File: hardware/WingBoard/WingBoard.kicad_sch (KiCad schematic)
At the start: 27 parts, among them J101 UPDI, J102 UART0, SW101 DIPA, SW103 SW_SPST, U101 ATmega4809-A

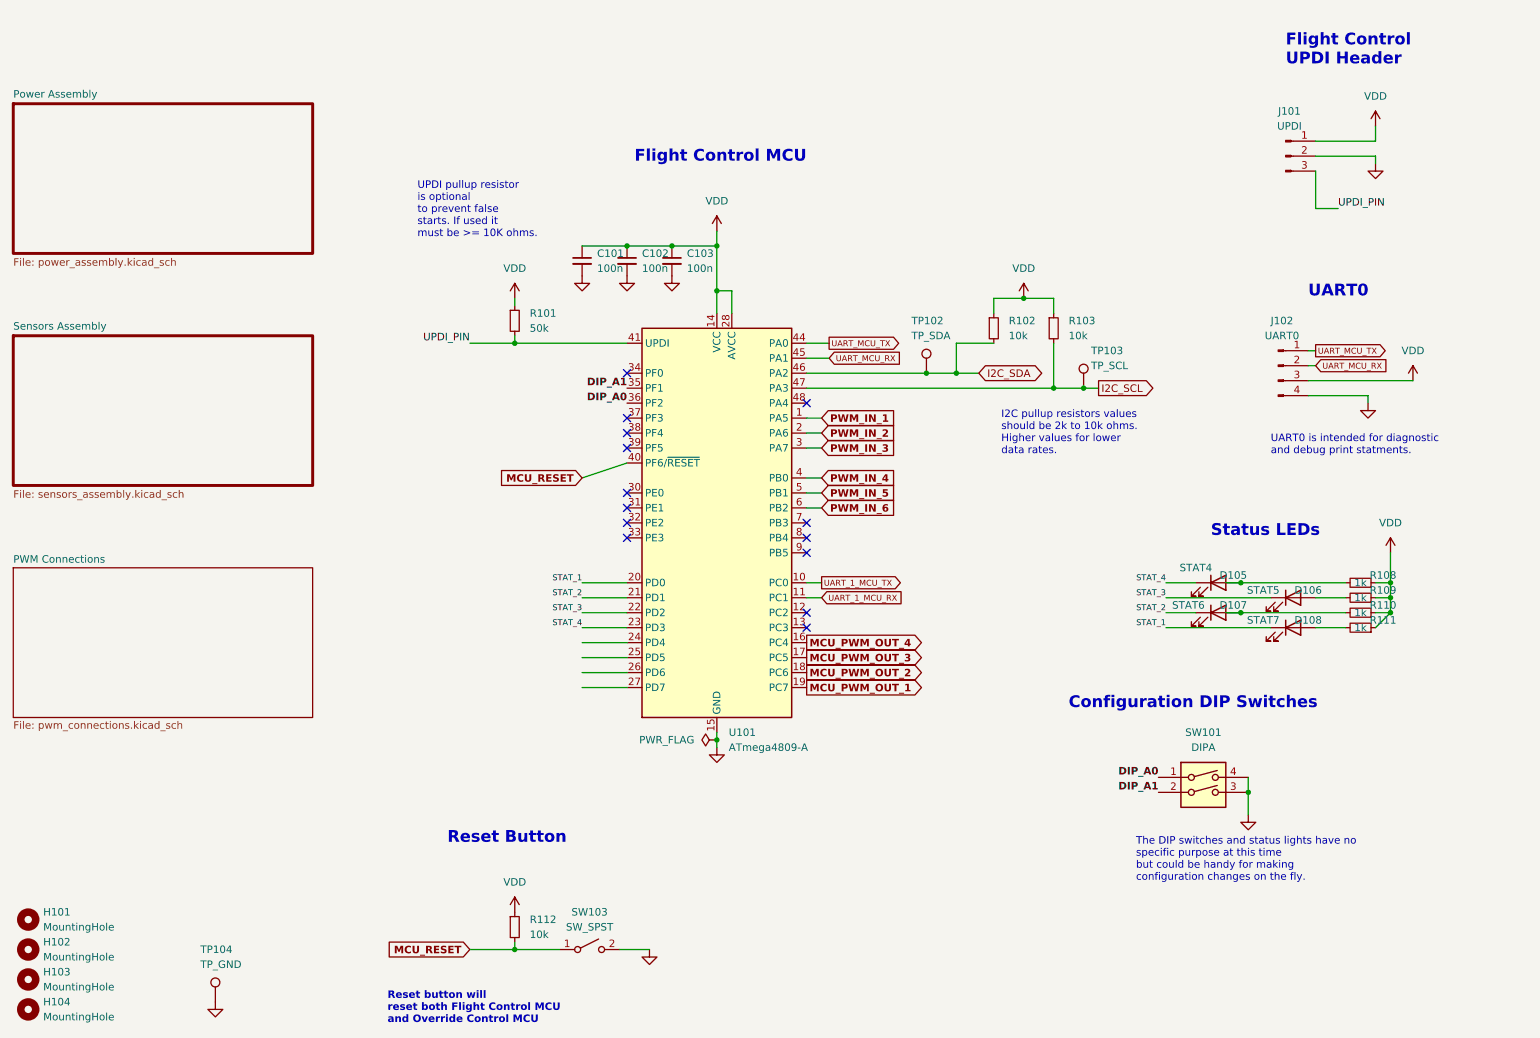
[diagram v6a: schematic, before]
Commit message: Final wingboard v0.1 hardware design.
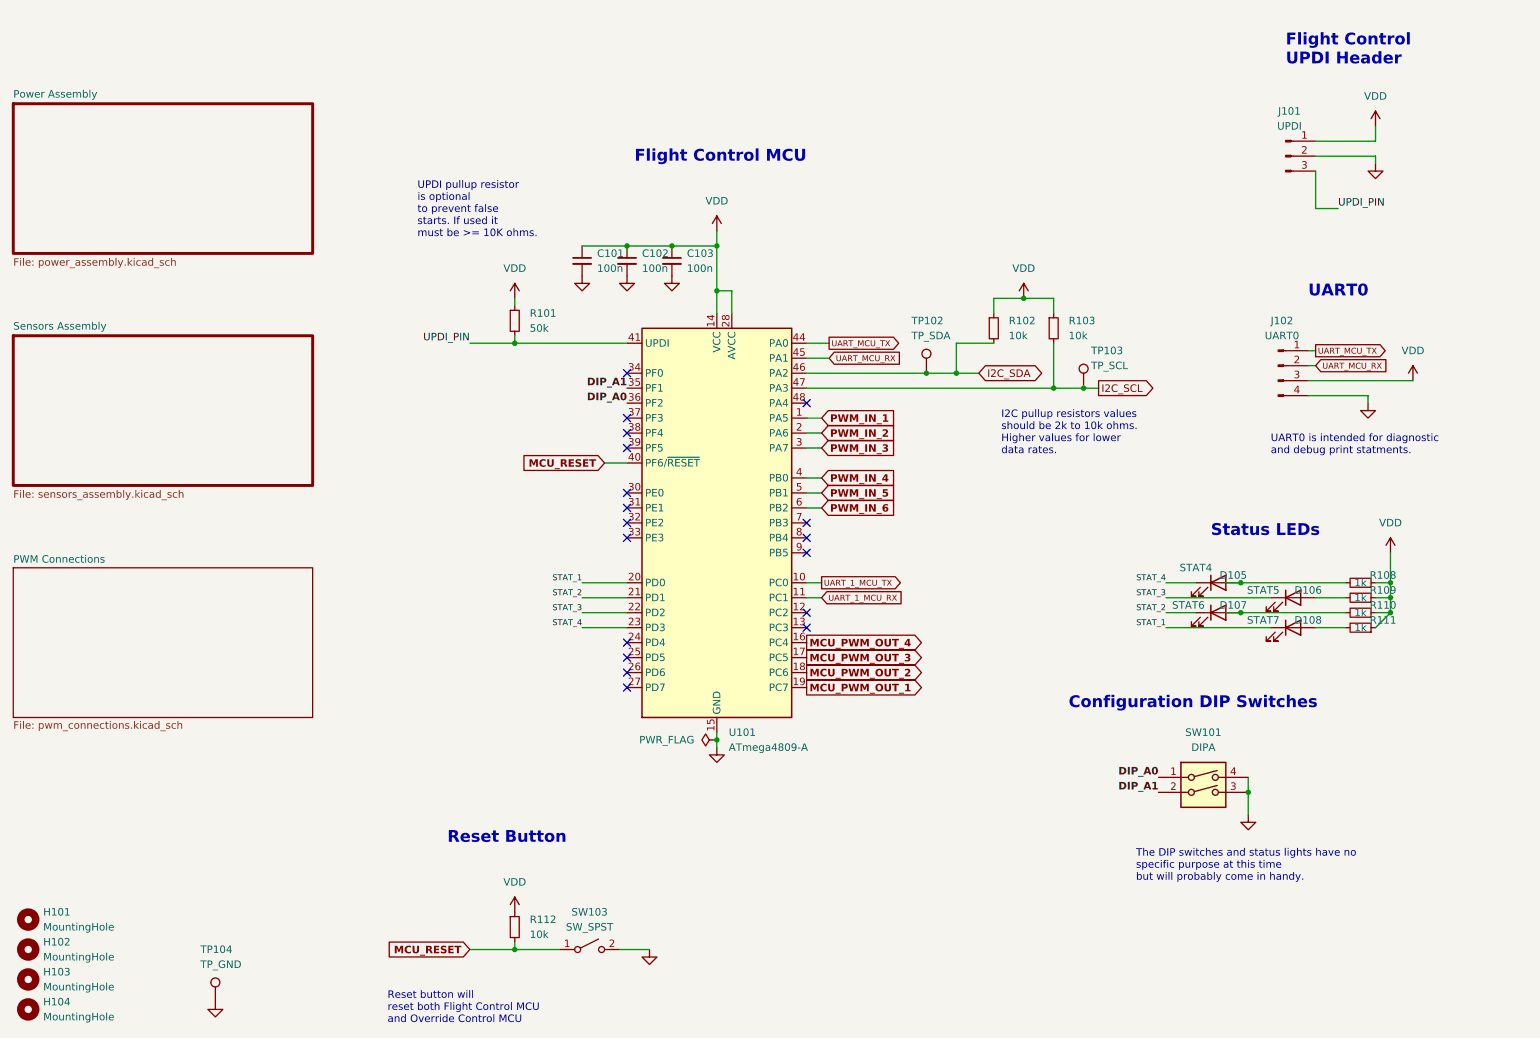
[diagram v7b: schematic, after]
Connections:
- no-connect marks 14 -> 18
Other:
- note added: "The DIP switches and status lights have no specific purpose at this time but will probably come in handy."
- note removed: "The DIP switches and status lights have no specific purpose at this time but could be handy for making configuration changes on the fly."
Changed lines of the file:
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@@
   (no_connect (at 172.72 107.95))
   (no_connect (at 172.72 118.11))
+  (no_connect (at 142.24 123.19))
+  (no_connect (at 142.24 125.73))
+  (no_connect (at 142.24 128.27))
+  (no_connect (at 142.24 130.81))
   (no_connect (at 142.24 85.09))
   (no_connect (at 142.24 87.63))
@@
     (stroke (width 0) (type default) (color 0 0 0 0))
   )
-  (wire (pts (xy 134.62 128.27) (xy 142.24 128.27))
-    (stroke (width 0) (type default) (color 0 0 0 0))
-  )
   (wire (pts (xy 267.97 82.55) (xy 267.97 81.28))
     (stroke (width 0) (type default) (color 0 0 0 0))
@@
     (stroke (width 0) (type default) (color 0 0 0 0))
   )
-  (wire (pts (xy 134.62 130.81) (xy 142.24 130.81))
-    (stroke (width 0) (type default) (color 0 0 0 0))
-  )
   (wire (pts (xy 233.68 115.57) (xy 251.46 115.57))
     (stroke (width 0) (type default) (color 0 0 0 0))
@@
     (stroke (width 0) (type default) (color 0 0 0 0))
   )
-  (wire (pts (xy 134.62 95.25) (xy 142.24 92.71))
+  (wire (pts (xy 138.43 92.71) (xy 142.24 92.71))
     (stroke (width 0) (type default) (color 0 0 0 0))
   )
@@
     (stroke (width 0) (type default) (color 0 0 0 0))
   )
-  (wire (pts (xy 134.62 123.19) (xy 142.24 123.19))
-    (stroke (width 0) (type default) (color 0 0 0 0))
-  )
   (wire (pts (xy 175.26 115.57) (xy 172.72 115.57))
     (stroke (width 0) (type default) (color 0 0 0 0))
@@
   )
   (wire (pts (xy 160.02 63.5) (xy 160.02 67.31))
-    (stroke (width 0) (type default) (color 0 0 0 0))
-  )
-  (wire (pts (xy 134.62 125.73) (xy 142.24 125.73))
     (stroke (width 0) (type default) (color 0 0 0 0))
   )
@@
     (effects (font (size 1.27 1.27)) (justify left bottom))
   )
-  (text "The DIP switches and status lights have no \nspecific purpose at this time\nbut could be handy for making \nconfiguration changes on the fly."
+  (text "The DIP switches and status lights have no \nspecific purpose at this time\nbut will probably come in handy."
     (at 228.6 163.83 0)
     (effects (font (size 1.27 1.27)) (justify left bottom))
@@
   (text "Reset button will\nreset both Flight Control MCU\nand Override Control MCU"
     (at 101.6 187.96 0)
-    (effects (font (size 1.27 1.27) bold) (justify left bottom))
+    (effects (font (size 1.27 1.27)) (justify left bottom))
   )
   (text "Flight Control\nUPDI Header" (at 254 25.4 0)
@@
     )
   )
-  (global_label "MCU_RESET" (shape input) (at 134.62 95.25 180) (fields_autoplaced)
+  (global_label "MCU_RESET" (shape input) (at 138.43 92.71 180) (fields_autoplaced)
     (effects (font (size 1.27 1.27) bold) (justify right))
-    (property "Intersheet References" "${INTERSHEET_REFS}" (id 0) (at 121.2517 95.123 0)
+    (property "Intersheet References" "${INTERSHEET_REFS}" (id 0) (at 125.0617 92.583 0)
       (effects (font (size 1.27 1.27) bold) (justify right) hide)
     )
